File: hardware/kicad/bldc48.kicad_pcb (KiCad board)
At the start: 4 copper layers, 170 x 100 mm, 172 parts, among them J1 BAT+, J10 BRAKE, J11 POWER_BTN, J12 UART, J2 BAT-, J3 MOTOR_A, J4 MOTOR_B, J5 MOTOR_C, J6 SWD, J7 HALL, J8 THROTTLE, J9 FWD/REV, Q1 MMBTA92, Q2 MMBTA42, Q3 IPT015N10N5, Q4 IPT015N10N5, Q5 IPT015N10N5, Q6 IPT015N10N5, Q7 IPT015N10N5, Q8 IPT015N10N5, U1 LM5164DDA, U10 STM32G431CBT6, U2 LM5164DDA, U3 AP2112K-3.3, U4 LM5109BMA, U5 INA240A2D, U6 LM5109BMA, U7 INA240A2D, U8 LM5109BMA, U9 INA240A2D

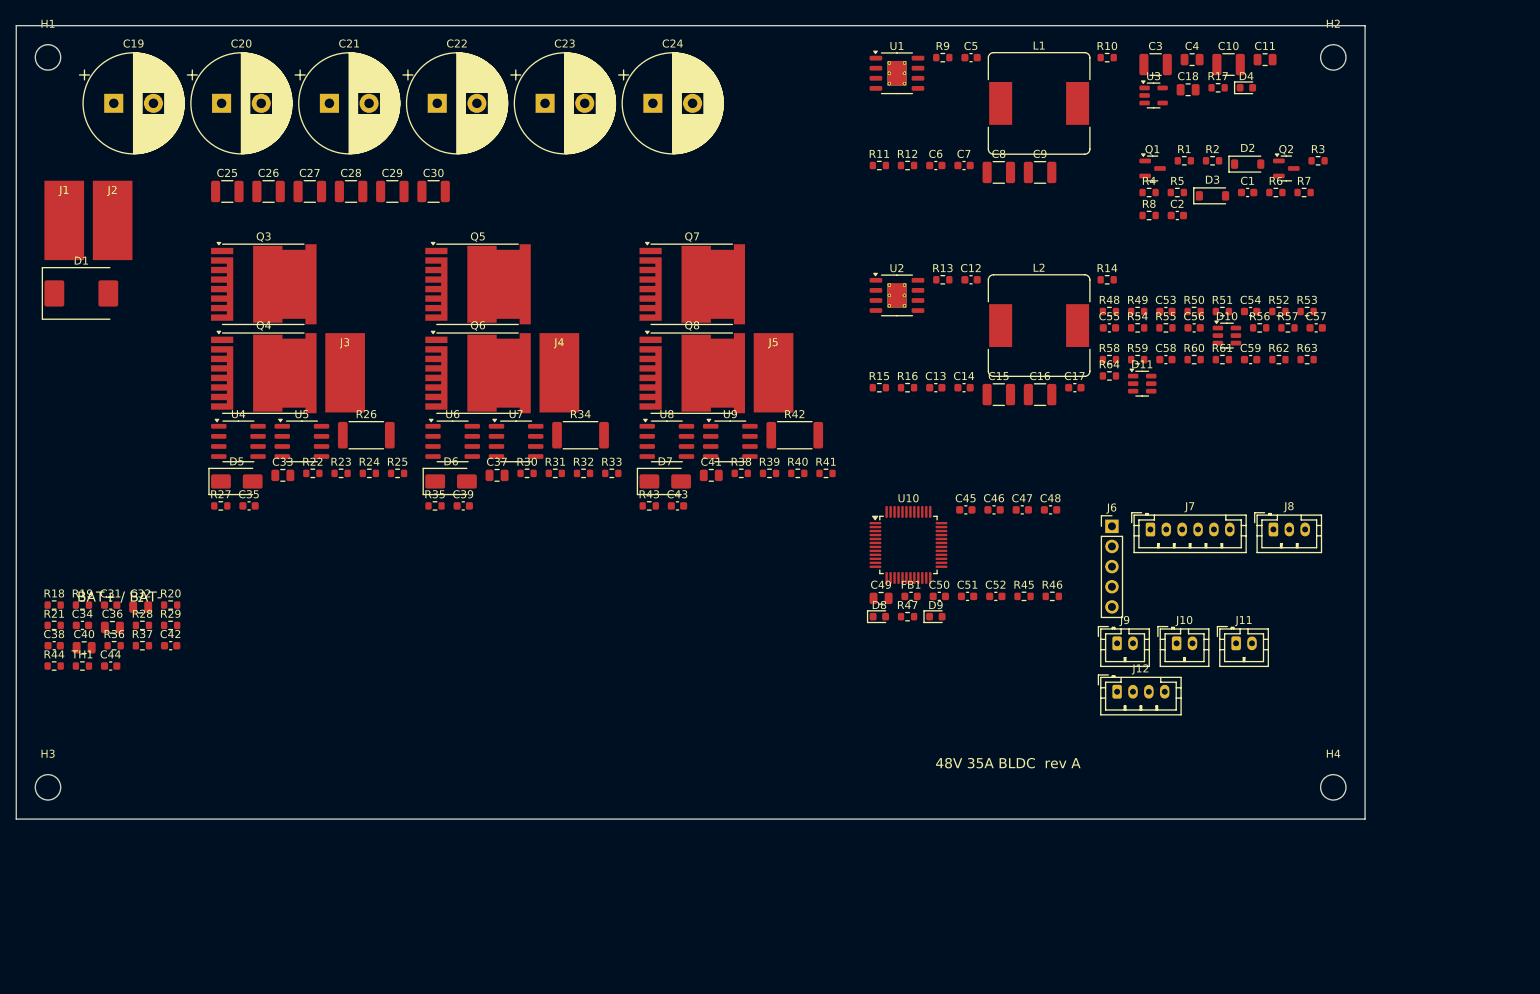
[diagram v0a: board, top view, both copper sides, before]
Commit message: Route the PCB and add 3D renders
- gen_pcb.py: structured placement (one column per phase: high/low FET,
  shunt, motor pad; driver and current amp alongside), 190x120 mm board,
  2 mm spacing for fan-out
- route_pcb.py: Specctra export, Freerouting (headless), own SES import
  (KiCad 7 has no scripted SES import) that restores layer-change vias the
  router omits, In1 GND / In2 +48V,+3V3 planes, outer-layer high-current
  pours, via arrays in power pads, zone fill + DRC
- routed board: 0 unconnected pads, 0 clearance errors in KiCad DRC
- render3d/: VRML export with KiCad 3D models + headless three.js renderer
- hardware/renders/: 3D views, routing and per-layer images, GLB model

Co-Authored-By: Claude Opus 5.5 <noreply@anthropic.com>
Claude-Session: https://claude.ai/code/session_01KE5bAkgcicsoh5erUtagKE
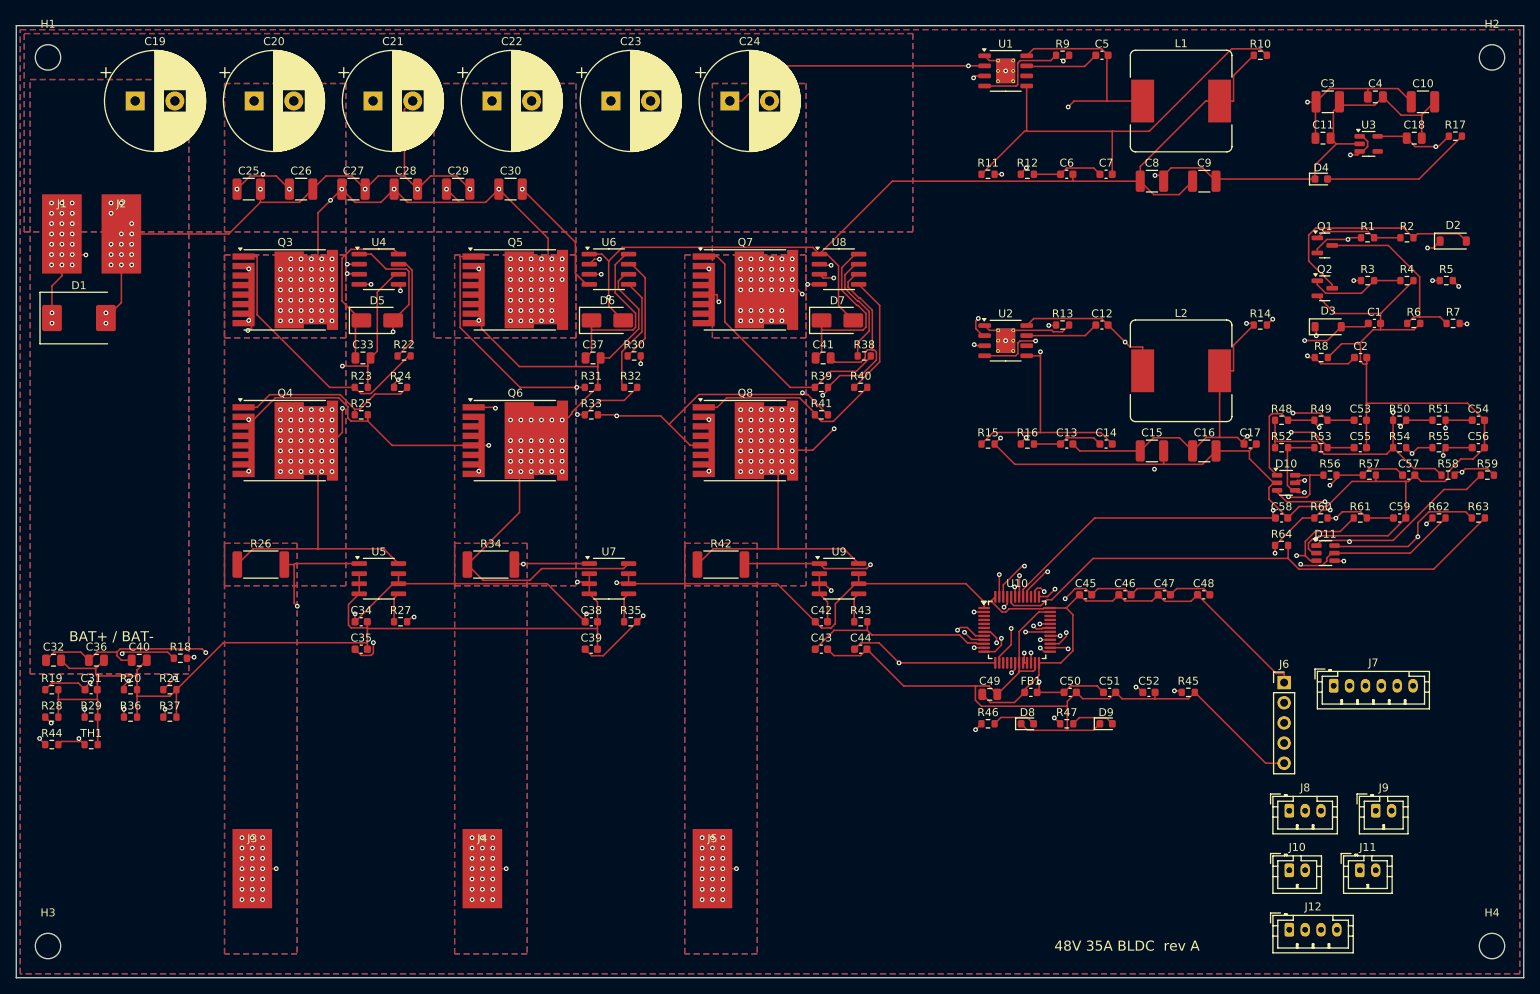
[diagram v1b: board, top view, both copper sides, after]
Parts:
- moved C44 94.6 mm to (106.4, 78.6)
- moved C42 82.1 mm to (101.5, 75.1)
- moved C38 67.8 mm to (72.5, 75.1)
- moved J3 63.6 mm to (29.7, 106.2)
- moved J4 63.2 mm to (58.7, 106.2)
- moved J5 63.0 mm to (87.7, 106.2)
- moved R59 46.4 mm to (185.4, 56.6)
- moved R58 45.1 mm to (180.5, 56.6)
- moved C56 38.9 mm to (184.3, 53.2)
- moved J9 38.8 mm to (171.3, 98.9)
- moved R55 37.6 mm to (179.3, 53.2)
- moved J12 37.0 mm to (160.4, 113.9)
- moved R54 36.3 mm to (174.4, 53.2)
- moved R5 35.7 mm to (180.2, 32.1)
- moved J8 35.5 mm to (160.4, 98.9)
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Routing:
- net GND: track 0.00 -> 1092.7 mm, vias 0 -> 43
- net +48V: track 0.00 -> 446.6 mm, vias 0 -> 151
- net +3V3: track 0.00 -> 371.0 mm, vias 0 -> 9
- net +12V: track 0.00 -> 245.4 mm, vias 0 -> 3
- net PWM_AH: track 0.00 -> 192.6 mm, vias 0 -> 3
- net PWM_AL: track 0.00 -> 183.0 mm, vias 0 -> 3
- net PWM_CH: track 0.00 -> 180.5 mm, vias 0 -> 3
- net PWM_CL: track 0.00 -> 178.4 mm, vias 0 -> 3
- net PWM_BH: track 0.00 -> 174.6 mm, vias 0 -> 3
- net PWM_BL: track 0.00 -> 167.8 mm, vias 0 -> 3
- net TEMP_FET: track 0.00 -> 131.5 mm, vias 0 -> 2
- net +5V: track 0.00 -> 130.8 mm, vias 0 -> 3
- net VBUS_SENSE: track 0.00 -> 122.3 mm, vias 0 -> 3
- net BUCK_EN: track 0.00 -> 108.6 mm, vias 0 -> 4
- net SW_C: track 0.00 -> 104.2 mm, vias 0 -> 46
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- added copper zone on In2.Cu, net +3V3
- added copper zone on B.Cu, net +48V
- added copper zone on F.Cu, net +48V
- added copper zone on In2.Cu, net +48V
- added copper zone on B.Cu, net GND
- added copper zone on F.Cu, net GND
- added copper zone on In1.Cu, net GND
- added copper zone on B.Cu, net PHASE_A
- added copper zone on F.Cu, net PHASE_A
- added copper zone on B.Cu, net PHASE_B
- added copper zone on F.Cu, net PHASE_B
- added copper zone on B.Cu, net PHASE_C
- added copper zone on F.Cu, net PHASE_C
- added copper zone on B.Cu, net SW_A
- added copper zone on F.Cu, net SW_A
- added copper zone on B.Cu, net SW_B
- added copper zone on F.Cu, net SW_B
- added copper zone on B.Cu, net SW_C
- added copper zone on F.Cu, net SW_C
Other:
- board size 170 x 100 mm -> 190 x 120 mm

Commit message: Rev B: fix power terminals and design-review findings
Layout (hand-placed power stage):
- BAT+/BAT- and MOTOR A/B/C are now M5 plated bolt terminals at the board
  edges (battery 36 mm apart on the left edge, motors under their shunts),
  replacing 5x10 mm SMD solder pads that sat 7.5 mm apart
- per phase: driver | high FET over low FET (drain tabs up, compact switch
  node) | Kelvin shunt + INA240; DC-link ceramics at the low-side sources
- FET NTC moved next to the middle low-side FET
- rule area keeps tracks off the inner planes under the power stage
- pours sized from real TOLL pad outlines; solid plane connections
- hand route for the one connection Freerouting leaves open; routing
  session saved so the board rebuilds without the autorouter
- KiCad DRC: 0 violations, 0 unconnected, footprints match library

Schematic / firmware:
- INA240A2 -> INA240A1: the 80 A hard trip was above the old +/-66 A ADC
  full scale and could never fire; compile-time assert + sim test added
- 4-terminal Kelvin shunts (BVR 4026) feed the INA240 sense inputs
- gate resistors 10R -> 4R7, bulk caps 6 -> 8

Co-Authored-By: Claude Opus 5.5 <noreply@anthropic.com>
Claude-Session: https://claude.ai/code/session_01KE5bAkgcicsoh5erUtagKE
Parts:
- added C60: 100n, Capacitor_SMD:C_0603_1608Metric, F.Cu at (224.3, 52.6)
- added C61: 100n, Capacitor_SMD:C_0603_1608Metric, F.Cu at (204.5, 56.0)
- C25, C26: value 2.2u/100V -> 220u/100V; footprint Capacitor_SMD:C_1210_3225Metric -> Capacitor_THT:CP_Radial_D12.5mm_P5.00mm
- C31: value 10n -> 2.2u/100V; footprint Capacitor_SMD:C_0603_1608Metric -> Capacitor_SMD:C_1210_3225Metric
- C32: value 1u/25V -> 2.2u/100V; footprint Capacitor_SMD:C_0805_2012Metric -> Capacitor_SMD:C_1210_3225Metric
- C33: value 2.2u/25V -> 10n; footprint Capacitor_SMD:C_0805_2012Metric -> Capacitor_SMD:C_0603_1608Metric
- C34, C38, C42: value 100n -> 1u/25V; footprint Capacitor_SMD:C_0603_1608Metric -> Capacitor_SMD:C_0805_2012Metric
- C35, C39, C43: value 1n -> 2.2u/25V; footprint Capacitor_SMD:C_0603_1608Metric -> Capacitor_SMD:C_0805_2012Metric
- C36, C40: value 1u/25V -> 100n; footprint Capacitor_SMD:C_0805_2012Metric -> Capacitor_SMD:C_0603_1608Metric
- C37, C41: value 2.2u/25V -> 1n; footprint Capacitor_SMD:C_0805_2012Metric -> Capacitor_SMD:C_0603_1608Metric
- C45, C56, C57: value 100n -> 1n
- C49: value 4.7u -> 100n; footprint Capacitor_SMD:C_0805_2012Metric -> Capacitor_SMD:C_0603_1608Metric
- C50: value 1u -> 100n
- C51: value 100n -> 4.7u; footprint Capacitor_SMD:C_0603_1608Metric -> Capacitor_SMD:C_0805_2012Metric
- C52: value 100n -> 1u
- C53, C54: value 1n -> 100n
- J1, J2, J3, J4, J5: footprint Connector_Wire:SolderWirePad_1x01_SMD_5x10mm -> MountingHole:MountingHole_5.3mm_M5_Pad_Via
- R22, R24, R30, R32, R38, R40: value 10R -> 4R7
- R26, R34, R42: footprint Resistor_SMD:R_2512_6332Metric -> Resistor_SMD:R_Shunt_Isabellenhuette_BVR4026
- U5, U7, U9: value INA240A2D -> INA240A1D
- moved C32 134.6 mm to (137.4, 57.5), turned to 90 degrees
- moved C46 131.3 mm to (8.44, 75.1)
- moved C31 124.0 mm to (130.6, 57.5), turned to 90 degrees
- moved C42 97.9 mm to (3.70, 71.4)
- moved C26 96.7 mm to (131.9, 9.49)
- moved C25 88.3 mm to (116.9, 9.49)
- moved C40 84.4 mm to (97.5, 59.7)
- moved TH1 83.3 mm to (88.0, 63.0)
- moved R52 75.4 mm to (234.2, 43.7)
- moved R46 73.5 mm to (195.7, 81.0)
- moved R56 70.4 mm to (235.4, 47.2)
- moved D10 70.4 mm to (229.8, 48.2)
- moved J10 69.3 mm to (225.2, 81.9)
- moved C38 69.2 mm to (3.70, 67.4)
- moved J5 68.0 mm to (154.0, 91.0)
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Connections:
- C31 pad 1: VBUS_SENSE -> +48V
- C32 pad 1: +12V -> +48V
- C33 pad 1: HB_A -> VBUS_SENSE
- C33 pad 2: SW_A -> GND
- C34 pad 1: +3V3 -> +12V
- C35 pad 1: ISENSE_A -> HB_A
- C35 pad 2: GND -> SW_A
- C36 pad 1: +12V -> +3V3
- C37 pad 1: HB_B -> ISENSE_A
- C37 pad 2: SW_B -> GND
- C38 pad 1: +3V3 -> +12V
- C39 pad 1: ISENSE_B -> HB_B
- C39 pad 2: GND -> SW_B
- C40 pad 1: +12V -> +3V3
- C41 pad 1: HB_C -> ISENSE_B
- C41 pad 2: SW_C -> GND
- C42 pad 1: +3V3 -> +12V
- C43 pad 1: ISENSE_C -> HB_C
- C43 pad 2: GND -> SW_C
- C44 pad 1: TEMP_FET -> +3V3
- C45 pad 1: +3V3 -> ISENSE_C
- C46 pad 1: +3V3 -> TEMP_FET
- C50 pad 1: +3V3A -> +3V3
- C51 pad 1: +3V3A -> +3V3
- C52 pad 1: NRST -> +3V3A
- C53 pad 1: HALL_A -> +3V3A
- C54 pad 1: HALL_B -> NRST
- C55 pad 1: HALL_C -> HALL_A
- C56 pad 1: TEMP_MOTOR -> HALL_B
- C57 pad 1: THROTTLE -> HALL_C
- C58 pad 1: DIR_SW -> TEMP_MOTOR
- C59 pad 1: BRAKE -> THROTTLE
- R26 pad 2: PHASE_A -> ISP_A
- R34 pad 2: PHASE_B -> ISP_B
- R42 pad 2: PHASE_C -> ISP_C
- U5 pad 1: PHASE_A -> ISN_A
- U5 pad 8: SW_A -> ISP_A
- U7 pad 1: PHASE_B -> ISN_B
- U7 pad 8: SW_B -> ISP_B
- U9 pad 1: PHASE_C -> ISN_C
- U9 pad 8: SW_C -> ISP_C
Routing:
- net +48V: track 446.6 -> 682.3 mm, vias 151 -> 144
- net +3V3: track 371.0 -> 519.7 mm, vias 9 -> 10
- net GND: track 1092.7 -> 1216.2 mm, vias 43 -> 33
- net +12V: track 245.4 -> 308.3 mm, vias 3 -> 0
- net VBUS_SENSE: track 122.3 -> 182.2 mm, vias 3 -> 2
- net SW_C: track 104.2 -> 46.4 mm, vias 46 -> 48
- net TEMP_FET: track 131.5 -> 185.5 mm, vias 2 -> 4
- net PWM_BL: track 167.8 -> 210.3 mm, vias 3 -> 4
- net SW_B: track 93.1 -> 53.6 mm, vias 32 -> 48
- net ISENSE_A: track 84.8 -> 123.8 mm, vias 3 -> 2
- net SW_A: track 85.6 -> 47.0 mm, vias 47 -> 48
- net PWM_BH: track 174.6 -> 207.4 mm
- net FB5: track 61.7 -> 31.0 mm, vias 2 -> 0
- net PWM_CL: track 178.4 -> 208.1 mm, vias 3 -> 4
- net PWM_AH: track 192.6 -> 220.9 mm
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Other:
- board size 190 x 120 mm -> 240 x 100 mm
- board text added: "48V 35A BLDC rev B"
- board text added: "BAT+"
- board text added: "BAT-"
- board text added: "MOTOR A"
- board text added: "MOTOR B"
- board text added: "MOTOR C"
- board text removed: "48V 35A BLDC rev A"
- board text removed: "BAT+ / BAT-"

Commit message: Rev C: compact 188x74 mm layout, re-routed, DRC clean; JLCPCB cost notes
- Repack the power stage into 38 mm phase columns and the logic into a 52 mm
  strip; smaller SRN8040TA buck inductors
- Re-route with Freerouting; record the LATCH_B hand route and move
  references that land on neighbouring silkscreen
- Regenerate BOM, schematic PDF, layer images and 3D renders (stand-in model
  for the SRN8040TA)
- README: rev C notes, phase-pour current capacity, JLCPCB cost estimate

Co-Authored-By: Claude Opus 5.5 <noreply@anthropic.com>
Claude-Session: https://claude.ai/code/session_01KE5bAkgcicsoh5erUtagKE
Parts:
- L1, L2: footprint Inductor_SMD:L_Bourns_SRR1260 -> Inductor_SMD:L_Bourns_SRN8040TA
- moved C11 94.7 mm to (138.4, 51.1)
- moved R3 93.7 mm to (147.1, 59.9)
- moved R7 91.2 mm to (147.1, 62.8)
- moved R6 90.7 mm to (142.7, 62.8)
- moved C1 90.2 mm to (138.2, 62.8)
- moved Q2 89.8 mm to (144.0, 55.9)
- moved R2 82.0 mm to (142.7, 59.9)
- moved R1 81.6 mm to (138.2, 59.9)
- moved D2 78.7 mm to (149.8, 55.4)
- moved C51 78.6 mm to (174.7, 3.23)
- moved D4 77.8 mm to (152.5, 50.9)
- moved R17 77.3 mm to (148.0, 50.9)
- moved C18 76.9 mm to (143.3, 51.1)
- moved C10 76.3 mm to (150.7, 46.8)
- moved D9 75.3 mm to (182.2, 9.98)
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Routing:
- net +48V: track 682.3 -> 504.6 mm, vias 144 -> 139
- net GND: track 1216.2 -> 1050.7 mm, vias 33 -> 20
- net PWM_BH: track 207.4 -> 357.1 mm, vias 3 -> 6
- net +3V3: track 519.7 -> 382.3 mm, vias 10 -> 8
- net +12V: track 308.3 -> 440.4 mm, vias 0 -> 2
- net PWM_BL: track 210.3 -> 336.3 mm, vias 4 -> 5
- net PWM_AL: track 207.4 -> 292.4 mm, vias 3 -> 6
- net ISENSE_B: track 79.1 -> 156.9 mm, vias 2 -> 3
- net PWM_CL: track 208.1 -> 279.2 mm, vias 4 -> 5
- net PHASE_B: track 78.7 -> 147.5 mm
- net ISENSE_C: track 29.8 -> 94.5 mm, vias 0 -> 4
- net ISENSE_A: track 123.8 -> 185.7 mm, vias 2 -> 3
- net PWM_CH: track 208.2 -> 269.6 mm, vias 3 -> 7
- net HALL_B: track 83.0 -> 24.3 mm, vias 3 -> 2
- net +5V: track 144.7 -> 90.6 mm, vias 5 -> 2
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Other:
- board size 240 x 100 mm -> 188 x 74 mm
- board text added: "48V 35A BLDC rev C"
- board text removed: "48V 35A BLDC rev B"
